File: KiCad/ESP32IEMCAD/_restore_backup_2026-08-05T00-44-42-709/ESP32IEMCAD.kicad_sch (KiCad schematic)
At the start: 0 parts

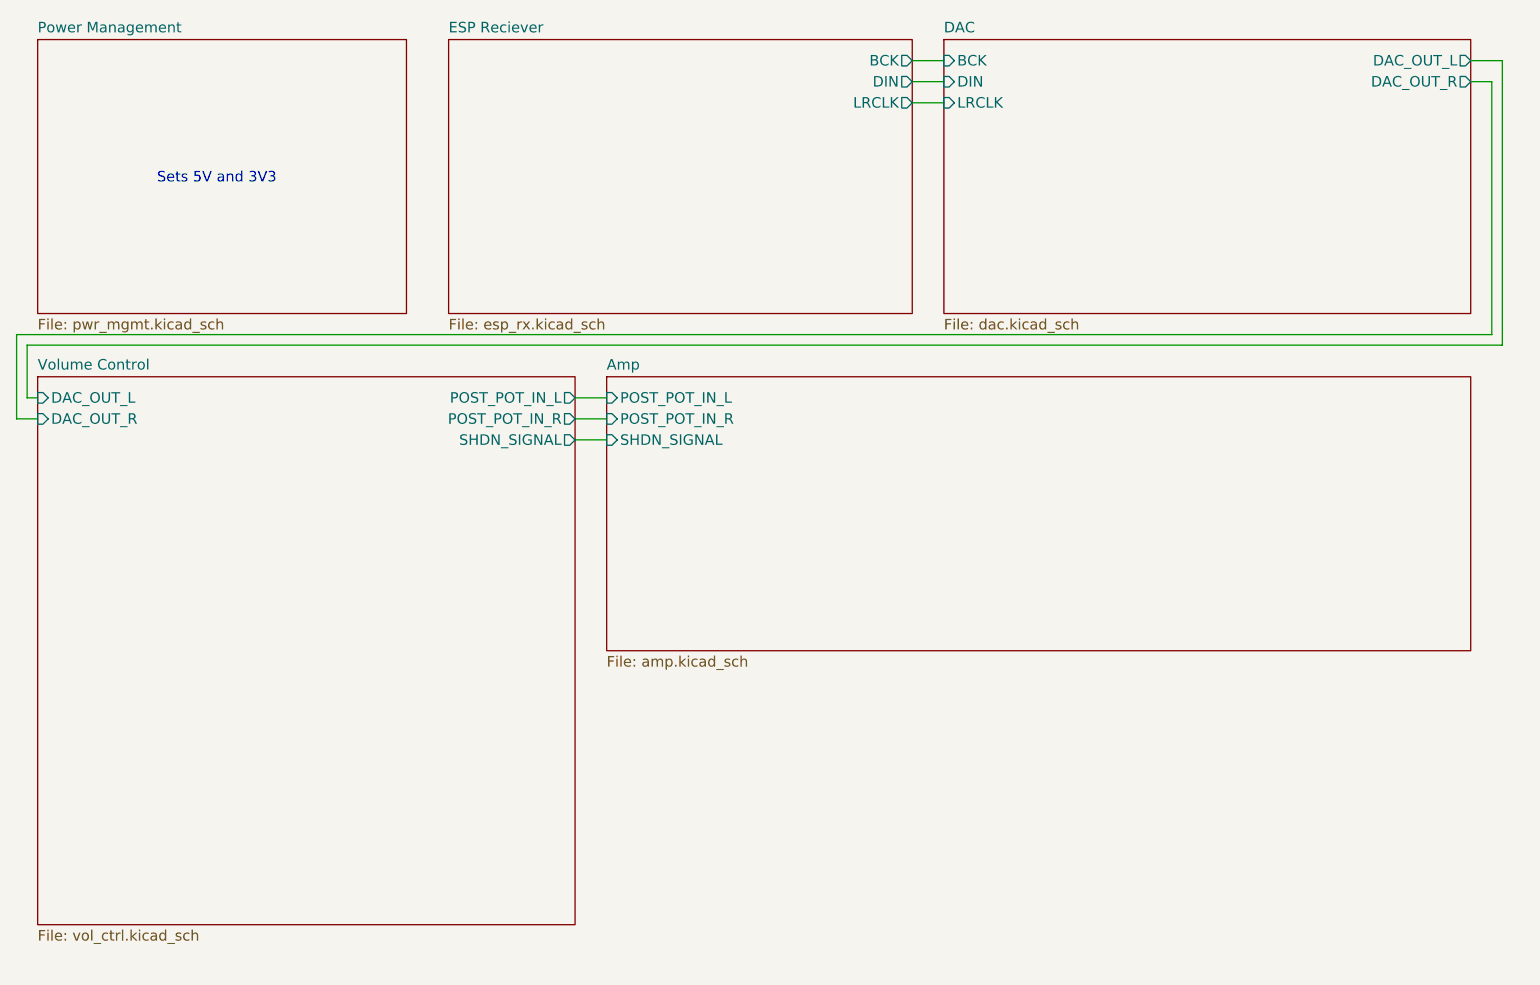
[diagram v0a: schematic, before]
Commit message: Resolved ERC errors.
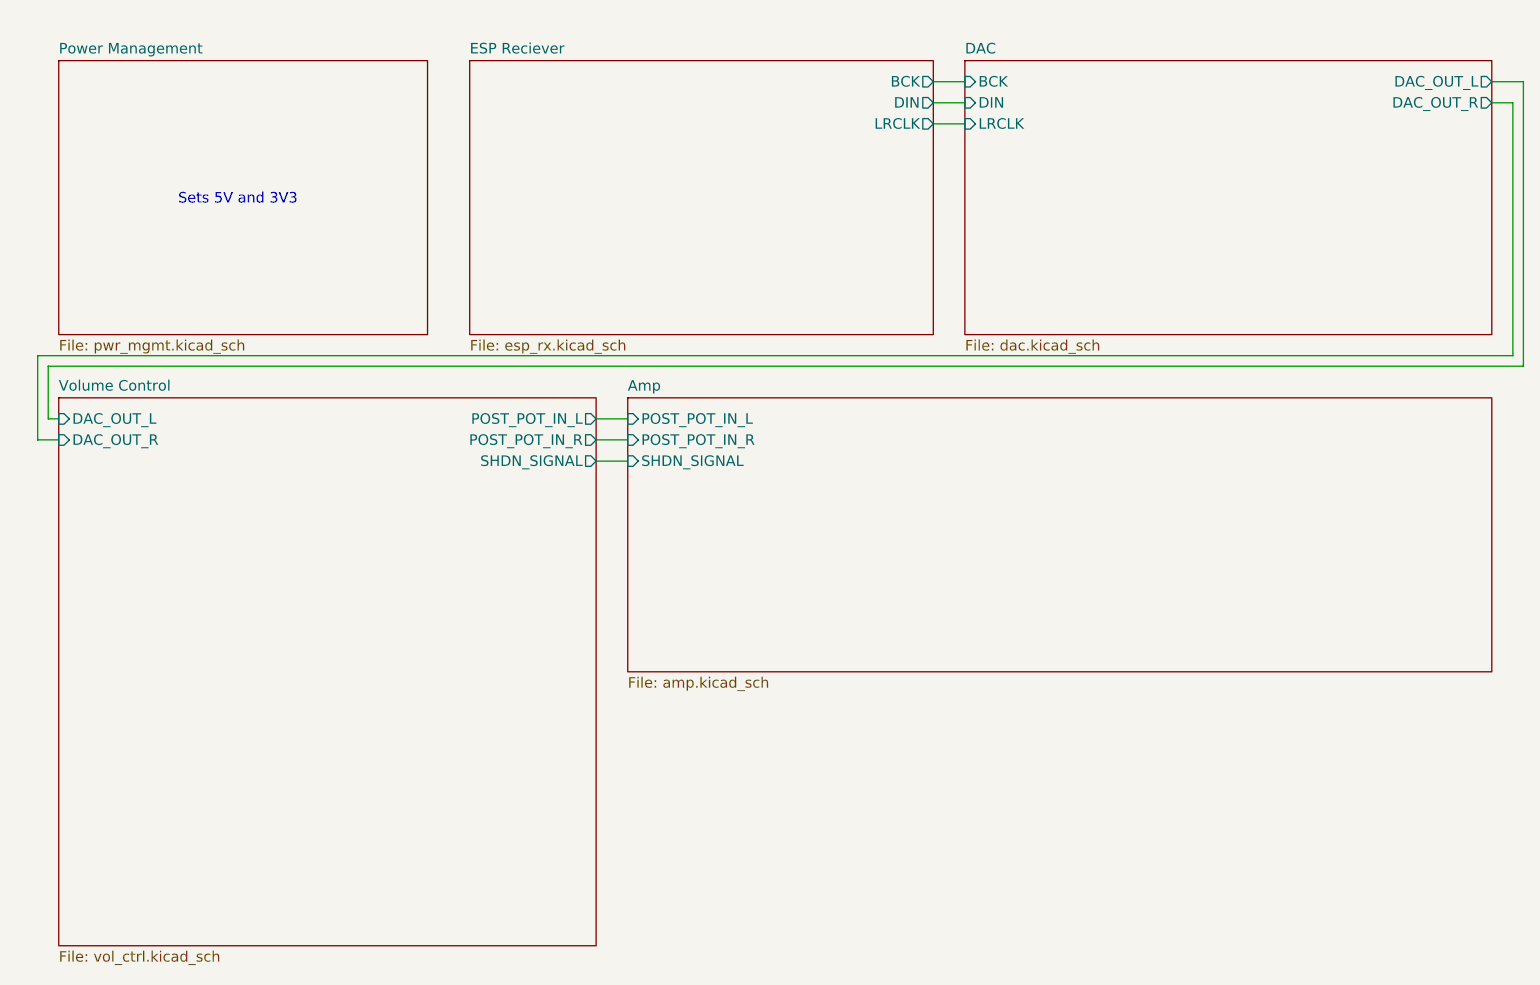
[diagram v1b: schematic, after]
